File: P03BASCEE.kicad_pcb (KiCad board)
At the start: 2 copper layers, 39.6 x 37.6 mm, 21 parts, among them J1 Serial, J2 Digital, J3 ICSP, J4 I2C, U1 24LC1025, U2 24LC1025, U3 DS13375+, U4 ATMEGA328P-AU, Y1 Crystal 32MHz, Y2 Crystal 16MHz

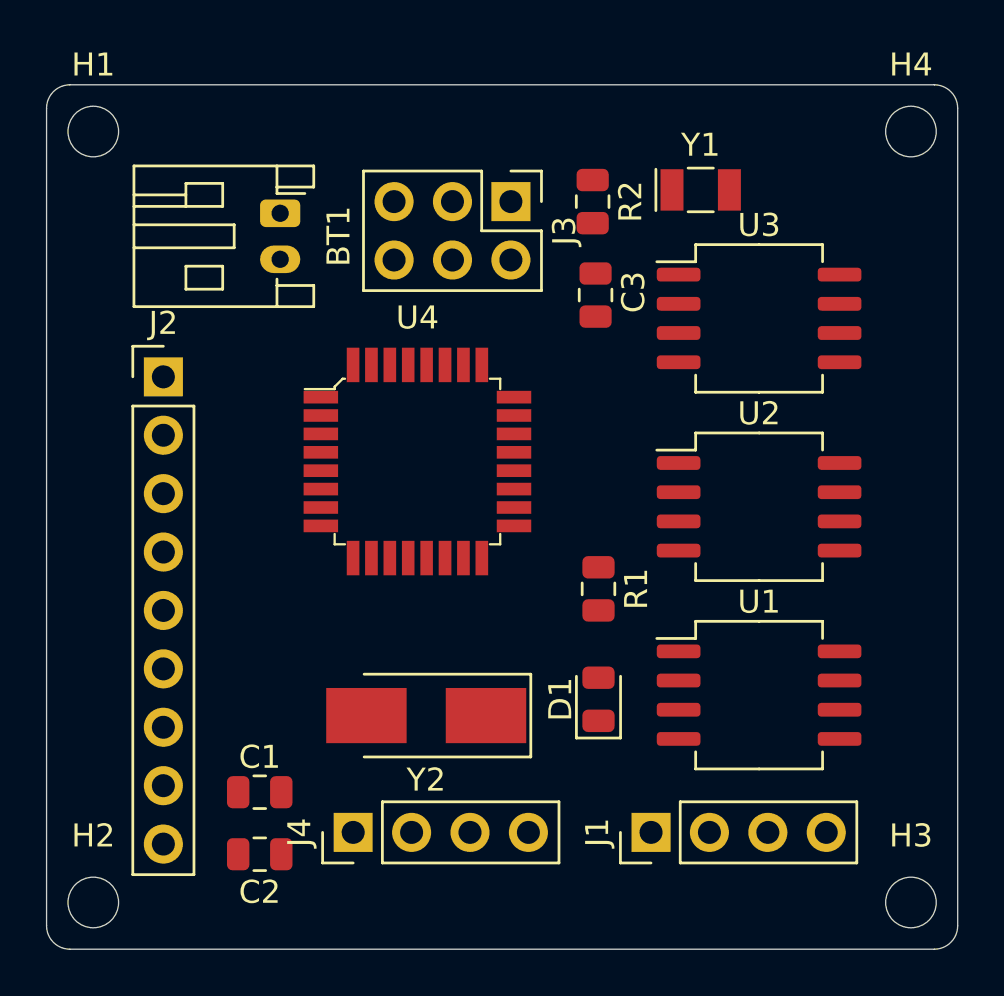
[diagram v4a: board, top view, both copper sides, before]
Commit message: Roteamento concluído para duas camadas
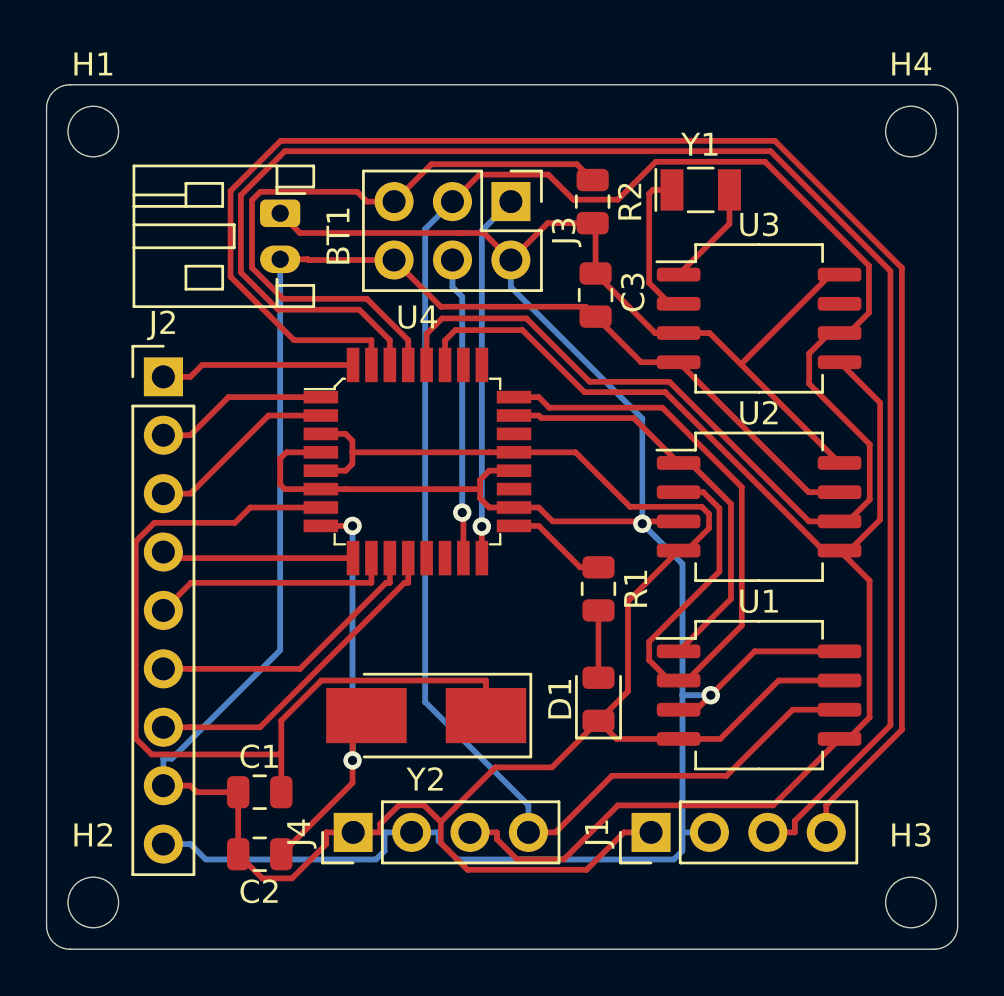
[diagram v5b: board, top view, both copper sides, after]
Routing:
- net GND: track 0.00 -> 135.1 mm
- net /VCC: track 0.00 -> 124.8 mm, vias 0 -> 2
- net /SCK: track 0.00 -> 104.9 mm
- net /RX: track 0.00 -> 70.6 mm
- net /TX: track 0.00 -> 70.4 mm
- net /SDA: track 0.00 -> 60.7 mm
- net Net-(C1-Pad1): track 0.00 -> 38.1 mm
- net /ADSS2: track 0.00 -> 32.9 mm
- net /RESET: track 0.00 -> 28.2 mm
- net Net-(C2-Pad1): track 0.00 -> 19.1 mm, vias 0 -> 2
- net /ADSS1: track 0.00 -> 18.4 mm
- net /MISO: track 0.00 -> 16.0 mm, vias 0 -> 1
- net /D8: track 0.00 -> 14.3 mm
- net /MOSI: track 0.00 -> 13.2 mm, vias 0 -> 1
- net /D7: track 0.00 -> 12.5 mm
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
